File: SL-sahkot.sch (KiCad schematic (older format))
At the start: 16 parts

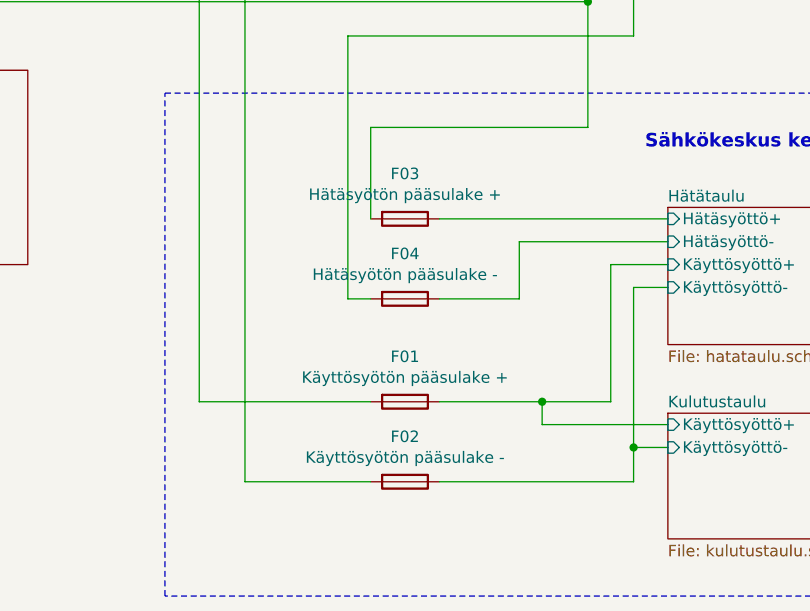
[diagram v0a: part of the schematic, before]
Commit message: IDitä muutettu osoitteistusluonnoksen mukaan
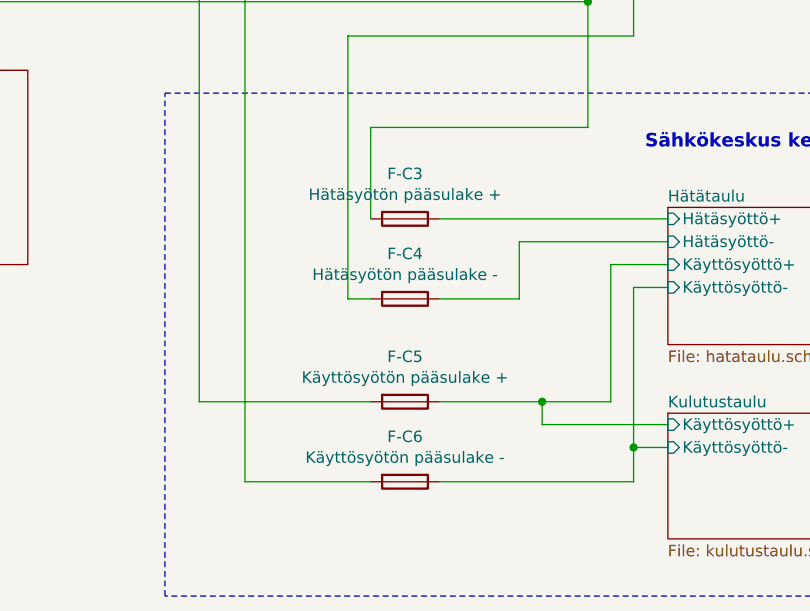
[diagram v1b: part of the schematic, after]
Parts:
- renumbered F03 to F-C3, F04 to F-C4, F01 to F-C5, F02 to F-C6
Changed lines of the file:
@@
 $EndSheet
 $Comp
-L Device:Fuse F01
+L Device:Fuse F-C5
 U 1 1 5DE9BAD4
 P 6350 4450
-F 0 "F01" V 6153 4450 50  0000 C CNN
+F 0 "F-C5" V 6153 4450 50  0000 C CNN
 F 1 "Käyttösyötön pääsulake +" V 6244 4450 50  0000 C CNN
 F 2 "" V 6280 4450 50  0001 C CNN
@@
 $EndComp
 $Comp
-L Device:Fuse F02
+L Device:Fuse F-C6
 U 1 1 5DE9C66F
 P 6350 4800
-F 0 "F02" V 6153 4800 50  0000 C CNN
+F 0 "F-C6" V 6153 4800 50  0000 C CNN
 F 1 "Käyttösyötön pääsulake -" V 6244 4800 50  0000 C CNN
 F 2 "" V 6280 4800 50  0001 C CNN
@@
 $EndComp
 $Comp
-L Device:Fuse F03
+L Device:Fuse F-C3
 U 1 1 5DE9CB20
 P 6350 3650
-F 0 "F03" V 6153 3650 50  0000 C CNN
+F 0 "F-C3" V 6153 3650 50  0000 C CNN
 F 1 "Hätäsyötön pääsulake +" V 6244 3650 50  0000 C CNN
 F 2 "" V 6280 3650 50  0001 C CNN
@@
 $EndComp
 $Comp
-L Device:Fuse F04
+L Device:Fuse F-C4
 U 1 1 5DE9CDD8
 P 6350 4000
-F 0 "F04" V 6153 4000 50  0000 C CNN
+F 0 "F-C4" V 6153 4000 50  0000 C CNN
 F 1 "Hätäsyötön pääsulake -" V 6244 4000 50  0000 C CNN
 F 2 "" V 6280 4000 50  0001 C CNN

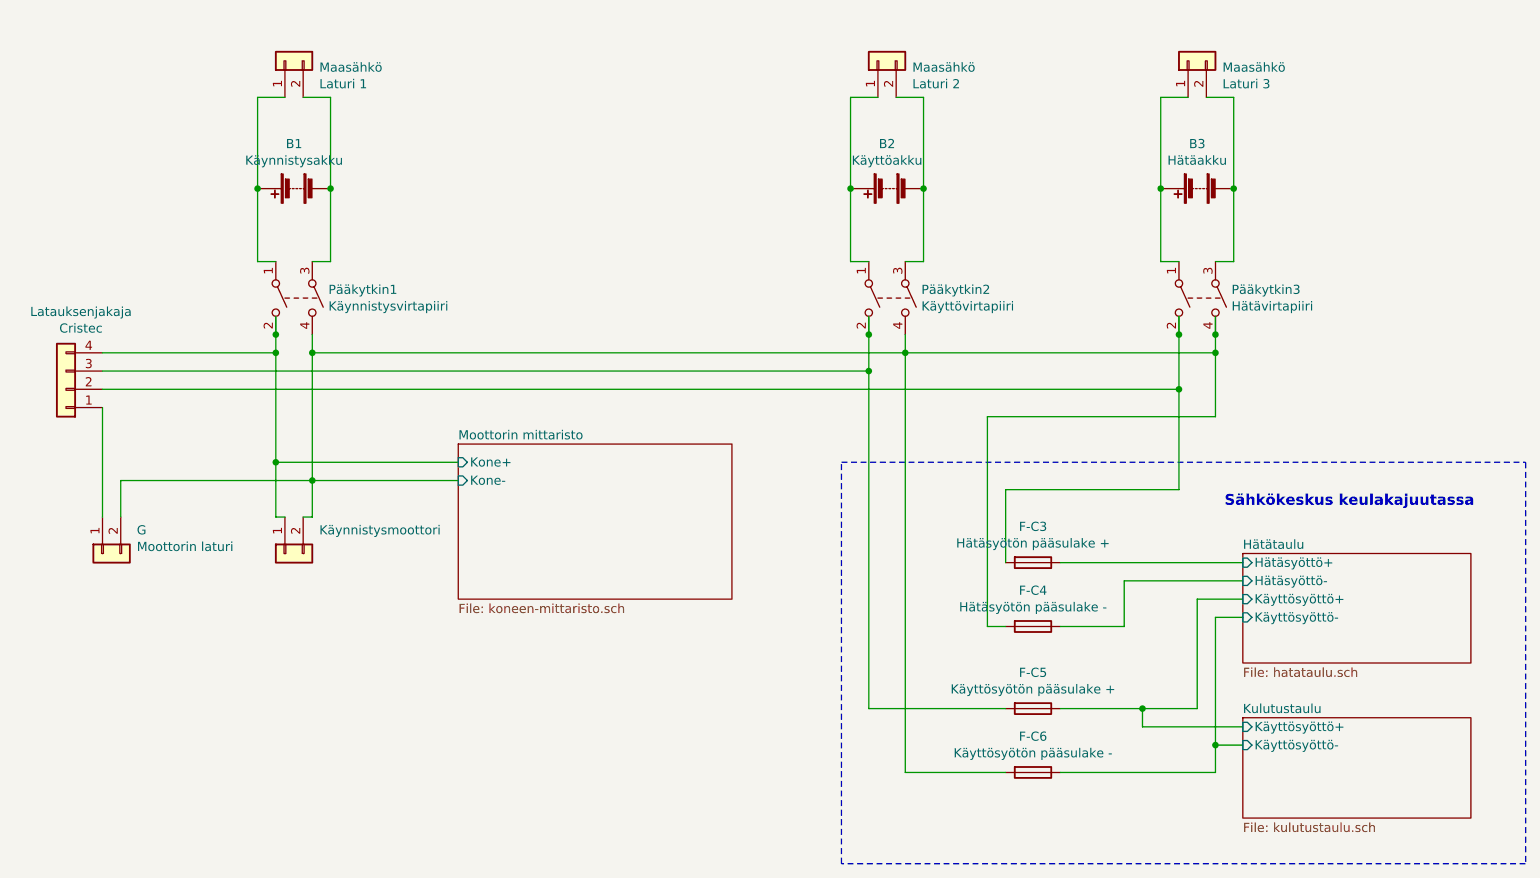
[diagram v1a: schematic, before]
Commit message: Komponenttien paikkojen ja johtojen reittien muutos yleiskuvaan
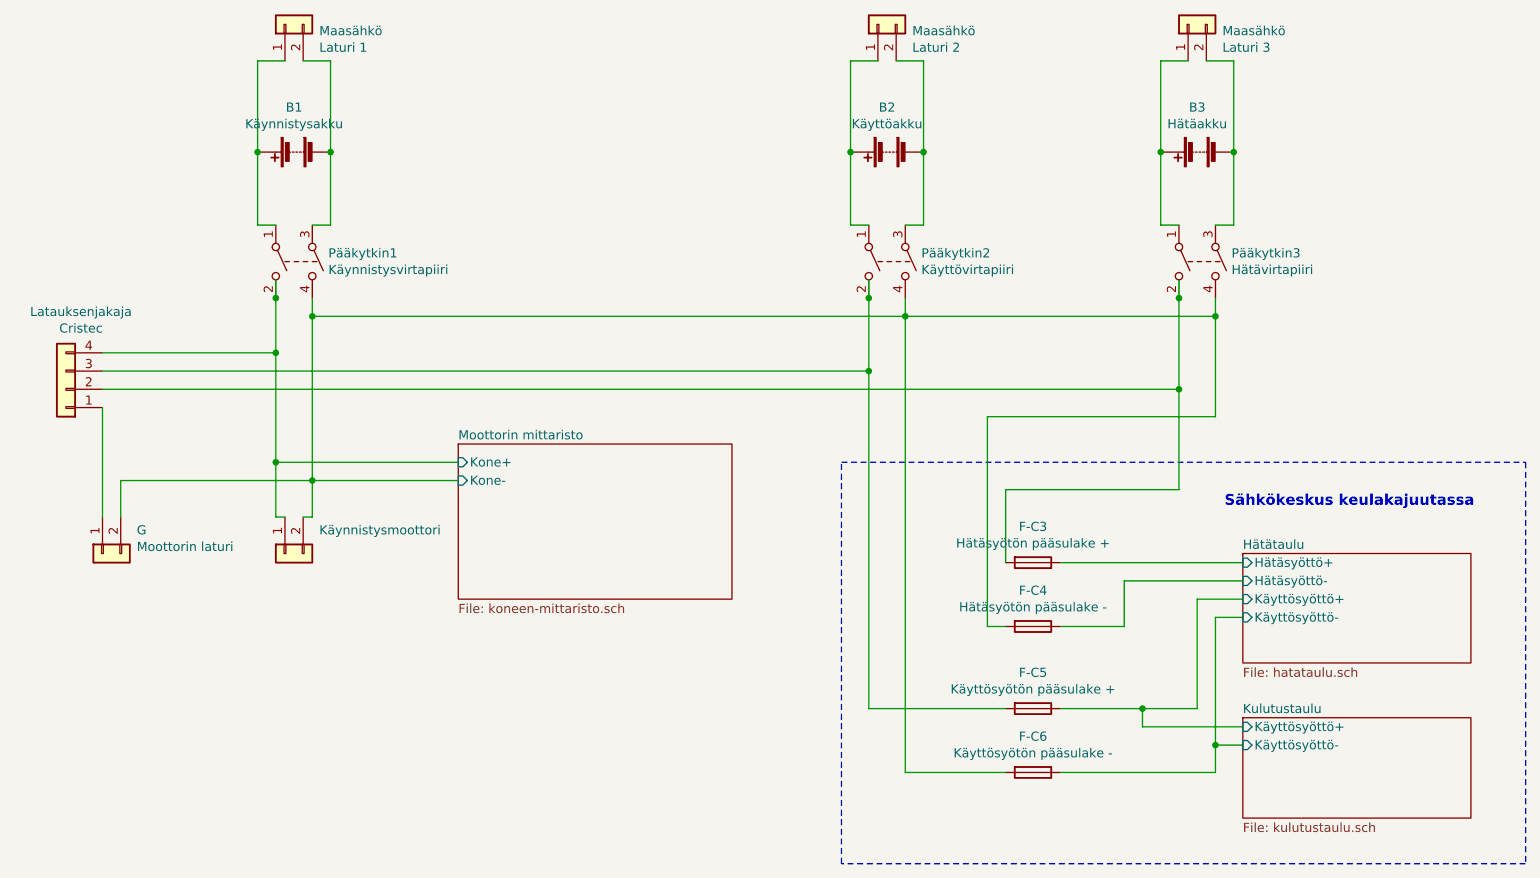
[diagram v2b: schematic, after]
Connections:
- wire segments 76 -> 75
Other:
- moved on the sheet: B1, B2, B3, Maasähkö, Pääkytkin1, Pääkytkin2, Pääkytkin3
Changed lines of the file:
@@
 L Device:Battery B1
 U 1 1 5DE04A3D
-P 2300 1600
-F 0 "B1" V 2055 1600 50  0000 C CNN
-F 1 "Käynnistysakku" V 2146 1600 50  0000 C CNN
-F 2 "" V 2300 1660 50  0001 C CNN
-F 3 "~" V 2300 1660 50  0001 C CNN
-	1    2300 1600
+P 2300 1400
+F 0 "B1" V 2055 1400 50  0000 C CNN
+F 1 "Käynnistysakku" V 2146 1400 50  0000 C CNN
+F 2 "" V 2300 1460 50  0001 C CNN
+F 3 "~" V 2300 1460 50  0001 C CNN
+	1    2300 1400
 	0    -1   1    0
 $EndComp
@@
 L Connector_Generic:Conn_01x02 Maasähkö
 U 1 1 5DE09D24
-P 2250 900
-F 0 "Maasähkö" V 2214 712 50  0000 R CNN
-F 1 "Laturi 1" V 2123 712 50  0000 R CNN
-F 2 "" H 2250 900 50  0001 C CNN
-F 3 "~" H 2250 900 50  0001 C CNN
-	1    2250 900
+P 2250 700
+F 0 "Maasähkö" V 2214 512 50  0000 R CNN
+F 1 "Laturi 1" V 2123 512 50  0000 R CNN
+F 2 "" H 2250 700 50  0001 C CNN
+F 3 "~" H 2250 700 50  0001 C CNN
+	1    2250 700
 	0    -1   -1   0
 $EndComp
 Wire Wire Line
-	2250 1100 2100 1100
-Wire Wire Line
-	2100 1100 2100 1600
-Wire Wire Line
-	2350 1100 2500 1100
-Wire Wire Line
-	2500 1100 2500 1600
+	2250 900  2100 900
+Wire Wire Line
+	2100 900  2100 1400
+Wire Wire Line
+	2350 900  2500 900
+Wire Wire Line
+	2500 900  2500 1400
 $Comp
 L Switch:SW_DPST Pääkytkin1
 U 1 1 5DE0B4D9
-P 2300 2200
-F 0 "Pääkytkin1" V 2254 2388 50  0000 L CNN
-F 1 "Käynnistysvirtapiiri" V 2345 2388 50  0000 L CNN
-F 2 "" H 2300 2200 50  0001 C CNN
-F 3 "~" H 2300 2200 50  0001 C CNN
-	1    2300 2200
-	0    1    1    0
-$EndComp
-Wire Wire Line
-	2100 1600 2100 2000
-Wire Wire Line
-	2100 2000 2200 2000
-Connection ~ 2100 1600
-Wire Wire Line
-	2500 1600 2500 2000
-Wire Wire Line
-	2500 2000 2400 2000
-Connection ~ 2500 1600
+P 2300 2000
+F 0 "Pääkytkin1" V 2254 2188 50  0000 L CNN
+F 1 "Käynnistysvirtapiiri" V 2345 2188 50  0000 L CNN
+F 2 "" H 2300 2000 50  0001 C CNN
+F 3 "~" H 2300 2000 50  0001 C CNN
+	1    2300 2000
+	0    1    1    0
+$EndComp
+Wire Wire Line
+	2100 1400 2100 1800
+Wire Wire Line
+	2100 1800 2200 1800
+Connection ~ 2100 1400
+Wire Wire Line
+	2500 1400 2500 1800
+Wire Wire Line
+	2500 1800 2400 1800
+Connection ~ 2500 1400
 $Comp
 L Connector_Generic:Conn_01x02 Käynnistysmoottori
@@
 	2400 3400 2350 3400
 Wire Wire Line
-	2200 2300 2200 2400
+	2200 2100 2200 2200
 Wire Wire Line
 	2200 3400 2250 3400
-Connection ~ 2200 2400
-Wire Wire Line
-	2200 2400 2200 2500
+Wire Wire Line
+	2200 2200 2200 2500
 $Comp
 L Connector_Generic:Conn_01x02 G
@@
 L Device:Battery B2
 U 1 1 5DE243CE
-P 5550 1600
-F 0 "B2" V 5305 1600 50  0000 C CNN
-F 1 "Käyttöakku" V 5396 1600 50  0000 C CNN
-F 2 "" V 5550 1660 50  0001 C CNN
-F 3 "~" V 5550 1660 50  0001 C CNN
-	1    5550 1600
+P 5550 1400
+F 0 "B2" V 5305 1400 50  0000 C CNN
+F 1 "Käyttöakku" V 5396 1400 50  0000 C CNN
+F 2 "" V 5550 1460 50  0001 C CNN
+F 3 "~" V 5550 1460 50  0001 C CNN
+	1    5550 1400
 	0    -1   1    0
 $EndComp
@@
 L Connector_Generic:Conn_01x02 Maasähkö
 U 1 1 5DE243D4
-P 5500 900
-F 0 "Maasähkö" V 5464 712 50  0000 R CNN
-F 1 "Laturi 2" V 5373 712 50  0000 R CNN
-F 2 "" H 5500 900 50  0001 C CNN
-F 3 "~" H 5500 900 50  0001 C CNN
-	1    5500 900
+P 5500 700
+F 0 "Maasähkö" V 5464 512 50  0000 R CNN
+F 1 "Laturi 2" V 5373 512 50  0000 R CNN
+F 2 "" H 5500 700 50  0001 C CNN
+F 3 "~" H 5500 700 50  0001 C CNN
+	1    5500 700
 	0    -1   -1   0
 $EndComp
 Wire Wire Line
-	5500 1100 5350 1100
-Wire Wire Line
-	5350 1100 5350 1600
-Wire Wire Line
-	5600 1100 5750 1100
-Wire Wire Line
-	5750 1100 5750 1600
+	5500 900  5350 900
+Wire Wire Line
+	5350 900  5350 1400
+Wire Wire Line
+	5600 900  5750 900
+Wire Wire Line
+	5750 900  5750 1400
 $Comp
 L Switch:SW_DPST Pääkytkin2
 U 1 1 5DE243DE
-P 5550 2200
-F 0 "Pääkytkin2" V 5504 2388 50  0000 L CNN
-F 1 "Käyttövirtapiiri" V 5595 2388 50  0000 L CNN
-F 2 "" H 5550 2200 50  0001 C CNN
-F 3 "~" H 5550 2200 50  0001 C CNN
-	1    5550 2200
-	0    1    1    0
-$EndComp
-Wire Wire Line
-	5350 1600 5350 2000
-Wire Wire Line
-	5350 2000 5450 2000
-Connection ~ 5350 1600
-Wire Wire Line
-	5750 1600 5750 2000
-Wire Wire Line
-	5750 2000 5650 2000
-Connection ~ 5750 1600
+P 5550 2000
+F 0 "Pääkytkin2" V 5504 2188 50  0000 L CNN
+F 1 "Käyttövirtapiiri" V 5595 2188 50  0000 L CNN
+F 2 "" H 5550 2000 50  0001 C CNN
+F 3 "~" H 5550 2000 50  0001 C CNN
+	1    5550 2000
+	0    1    1    0
+$EndComp
+Wire Wire Line
+	5350 1400 5350 1800
+Wire Wire Line
+	5350 1800 5450 1800
+Connection ~ 5350 1400
+Wire Wire Line
+	5750 1400 5750 1800
+Wire Wire Line
+	5750 1800 5650 1800
+Connection ~ 5750 1400
 $Comp
 L Device:Battery B3
 U 1 1 5DE26C97
-P 7250 1600
-F 0 "B3" V 7005 1600 50  0000 C CNN
-F 1 "Hätäakku" V 7096 1600 50  0000 C CNN
-F 2 "" V 7250 1660 50  0001 C CNN
-F 3 "~" V 7250 1660 50  0001 C CNN
-	1    7250 1600
+P 7250 1400
+F 0 "B3" V 7005 1400 50  0000 C CNN
+F 1 "Hätäakku" V 7096 1400 50  0000 C CNN
+F 2 "" V 7250 1460 50  0001 C CNN
+F 3 "~" V 7250 1460 50  0001 C CNN
+	1    7250 1400
 	0    -1   1    0
 $EndComp
@@
 L Connector_Generic:Conn_01x02 Maasähkö
 U 1 1 5DE26C9D
-P 7200 900
-F 0 "Maasähkö" V 7164 712 50  0000 R CNN
-F 1 "Laturi 3" V 7073 712 50  0000 R CNN
-F 2 "" H 7200 900 50  0001 C CNN
-F 3 "~" H 7200 900 50  0001 C CNN
-	1    7200 900
+P 7200 700
+F 0 "Maasähkö" V 7164 512 50  0000 R CNN
+F 1 "Laturi 3" V 7073 512 50  0000 R CNN
+F 2 "" H 7200 700 50  0001 C CNN
+F 3 "~" H 7200 700 50  0001 C CNN
+	1    7200 700
 	0    -1   -1   0
 $EndComp
 Wire Wire Line
-	7200 1100 7050 1100
-Wire Wire Line
-	7050 1100 7050 1600
-Wire Wire Line
-	7300 1100 7450 1100
-Wire Wire Line
-	7450 1100 7450 1600
+	7200 900  7050 900
+Wire Wire Line
+	7050 900  7050 1400
+Wire Wire Line
+	7300 900  7450 900
+Wire Wire Line
+	7450 900  7450 1400
 $Comp
 L Switch:SW_DPST Pääkytkin3
 U 1 1 5DE26CA7
-P 7250 2200
-F 0 "Pääkytkin3" V 7204 2388 50  0000 L CNN
-F 1 "Hätävirtapiiri" V 7295 2388 50  0000 L CNN
-F 2 "" H 7250 2200 50  0001 C CNN
-F 3 "~" H 7250 2200 50  0001 C CNN
-	1    7250 2200
-	0    1    1    0
-$EndComp
-Wire Wire Line
-	7050 1600 7050 2000
-Wire Wire Line
-	7050 2000 7150 2000
-Connection ~ 7050 1600
-Wire Wire Line
-	7450 1600 7450 2000
-Wire Wire Line
-	7450 2000 7350 2000
-Connection ~ 7450 1600
-Wire Wire Line
-	5650 2500 5650 2400
-Wire Wire Line
-	5650 2500 7350 2500
-Connection ~ 5650 2500
-Wire Wire Line
-	5450 2300 5450 2400
-Connection ~ 5450 2400
-Wire Wire Line
-	5450 2400 5450 2600
-Wire Wire Line
-	7150 2300 7150 2400
-Connection ~ 7150 2400
-Wire Wire Line
-	7150 2400 7150 2700
-Wire Wire Line
-	7350 2300 7350 2400
-Connection ~ 7350 2400
-Wire Wire Line
-	7350 2400 7350 2500
+P 7250 2000
+F 0 "Pääkytkin3" V 7204 2188 50  0000 L CNN
+F 1 "Hätävirtapiiri" V 7295 2188 50  0000 L CNN
+F 2 "" H 7250 2000 50  0001 C CNN
+F 3 "~" H 7250 2000 50  0001 C CNN
+	1    7250 2000
+	0    1    1    0
+$EndComp
+Wire Wire Line
+	7050 1400 7050 1800
+Wire Wire Line
+	7050 1800 7150 1800
+Connection ~ 7050 1400
+Wire Wire Line
+	7450 1400 7450 1800
+Wire Wire Line
+	7450 1800 7350 1800
+Connection ~ 7450 1400
+Wire Wire Line
+	5650 2300 7350 2300
+Connection ~ 5650 2300
+Wire Wire Line
+	5450 2100 5450 2200
 $Sheet
 S 7500 3600 1250 600
@@
 	6100 2850 7350 2850
 Wire Wire Line
-	7350 2850 7350 2500
-Connection ~ 7350 2500
+	7350 2850 7350 2300
 Wire Wire Line
 	6200 4800 5650 4800
@@
 $EndSheet
 Wire Wire Line
-	2400 2500 5650 2500
-Wire Wire Line
-	2400 2400 2400 2500
-Connection ~ 2400 2500
-Wire Wire Line
-	2400 2500 2400 3200
+	2400 2300 5650 2300
 Wire Wire Line
 	1250 2600 5450 2600
@@
 	7150 2700 7150 3250
 Wire Wire Line
-	5650 2500 5650 4800
-Connection ~ 5450 2600
+	5650 2300 5650 4800
 Wire Wire Line
 	5450 2600 5450 4450
@@
 Text Notes 7400 3350 0    59   ~ 12
 Sähkökeskus keulakajuutassa
+Connection ~ 2200 2200
+Wire Wire Line
+	7150 2100 7150 2200
+Wire Wire Line
+	7150 2200 7150 2700
+Connection ~ 7150 2200
+Wire Wire Line
+	5450 2200 5450 2600
+Connection ~ 5450 2200
+Connection ~ 5450 2600
+Wire Wire Line
+	2400 2300 2400 3200
+Wire Wire Line
+	2400 2200 2400 2300
+Connection ~ 2400 2300
+Wire Wire Line
+	5650 2200 5650 2300
+Wire Wire Line
+	7350 2200 7350 2300
+Connection ~ 7350 2300
 $EndSCHEMATC
